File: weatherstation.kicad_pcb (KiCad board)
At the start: 2 copper layers, 53.3 x 53.3 mm, 29 parts, among them J1 Conn_02x13_Odd_Even, J10 Conn_01x03_Male, J2 Conn_01x02_Male, J3 Conn_01x02_Male, J4 Conn_01x02_Male, J5 Conn_01x02_Male, J6 Conn_01x02_Male, J7 Conn_01x02_Male, J8 Conn_01x02_Male, J9 Conn_01x02_Male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

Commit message: Added logo. Tidied up a bit
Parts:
- added G***: LOGO, logodir:mylogo small, F.Cu at (163.8, 115.6)
- moved J2 1.27 mm to (166.4, 108.0)
- moved J10 0.37 mm to (166.4, 94.0)
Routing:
- net GND: track 236.4 -> 263.9 mm
- net /Dir-: track 93.4 -> 88.6 mm
- net Net-(D1-Pad1): track 36.8 -> 35.1 mm
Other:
- board text added: "+"
- board text added: "-"
- board text added: "Anemometer"
- board text added: "Direction Vane"
- board text added: "Weather Station"

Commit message: Changed name
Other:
- board text added: "eWx1"
- board text removed: "Layout V2"
- board text removed: "Weather Station"

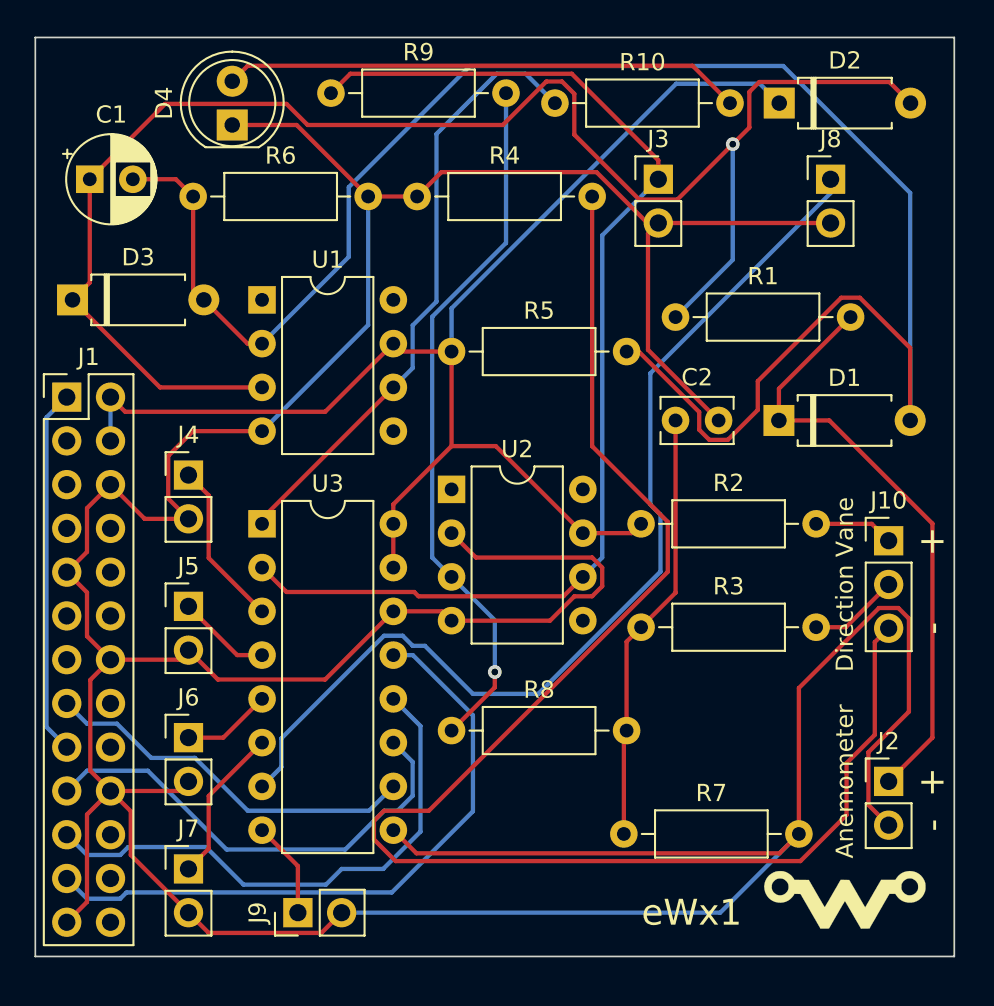
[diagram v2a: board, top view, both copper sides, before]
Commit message: Fixed backwards raspi header
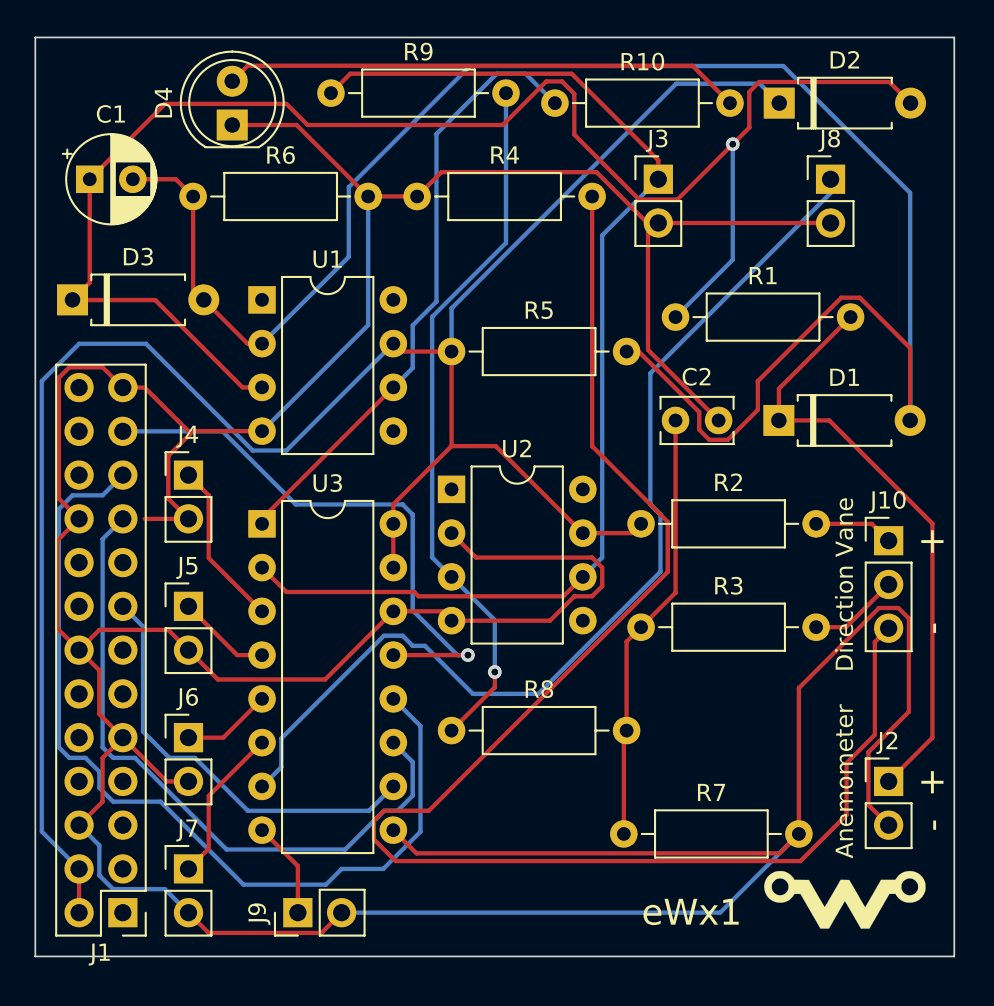
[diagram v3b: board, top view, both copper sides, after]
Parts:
- moved J1 30.1 mm to (121.9, 115.6), turned to 180 degrees
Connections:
- J1 pad 1: +3V3 -> Net-(J1-Pad1)
- J1 pad 17: +3V3 -> Net-(J1-Pad17)
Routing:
- net +5V: track 79.2 -> 116.4 mm
- net +3V3: track 21.3 -> 0.00 mm
- net /ADC_Dout: track 31.7 -> 52.8 mm
- net /ADC_Din: track 27.3 -> 39.0 mm
- net GND: track 263.9 -> 275.5 mm
- net /ADC_CLK: track 37.8 -> 33.0 mm, vias 0 -> 1
- net /ADC_CS: track 22.1 -> 24.8 mm
